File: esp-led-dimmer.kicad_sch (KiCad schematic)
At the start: 7 parts, among them J1 Barrel_Jack, J2 ESP-01, U1 LM2594M-3.3

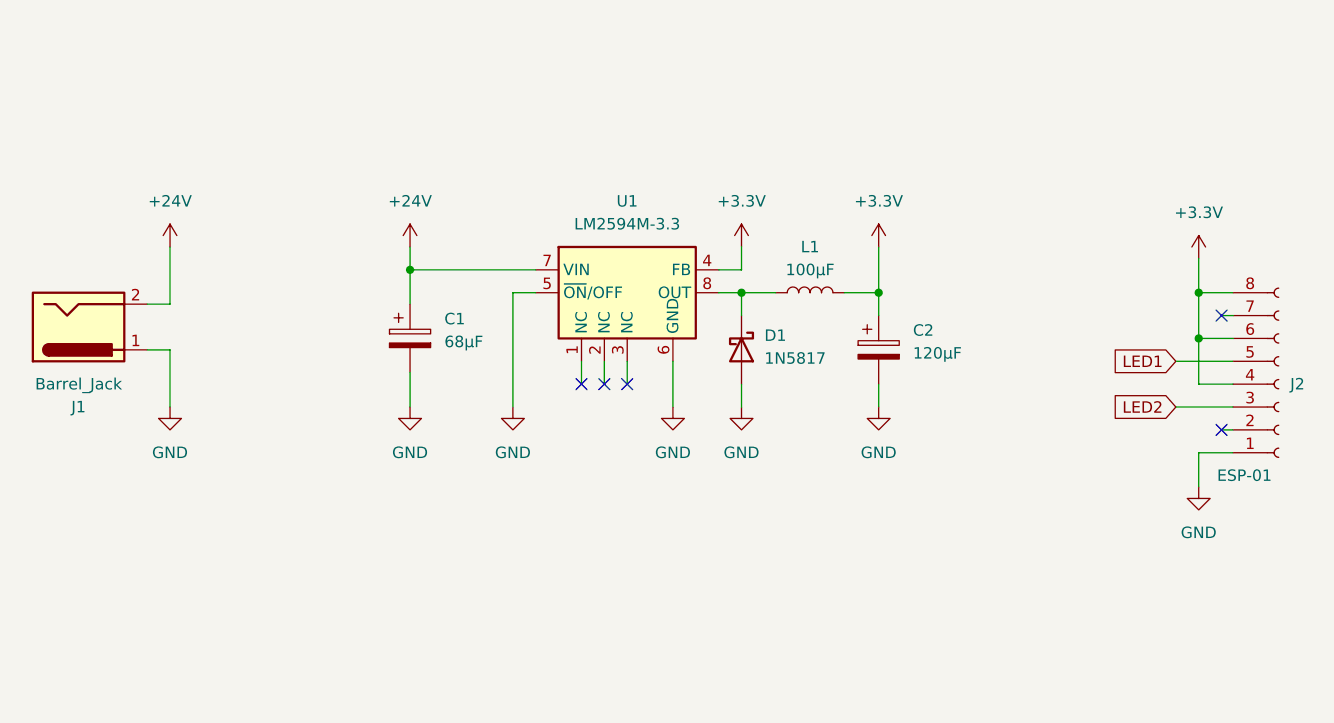
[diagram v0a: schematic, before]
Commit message: Add LED dimming circuit
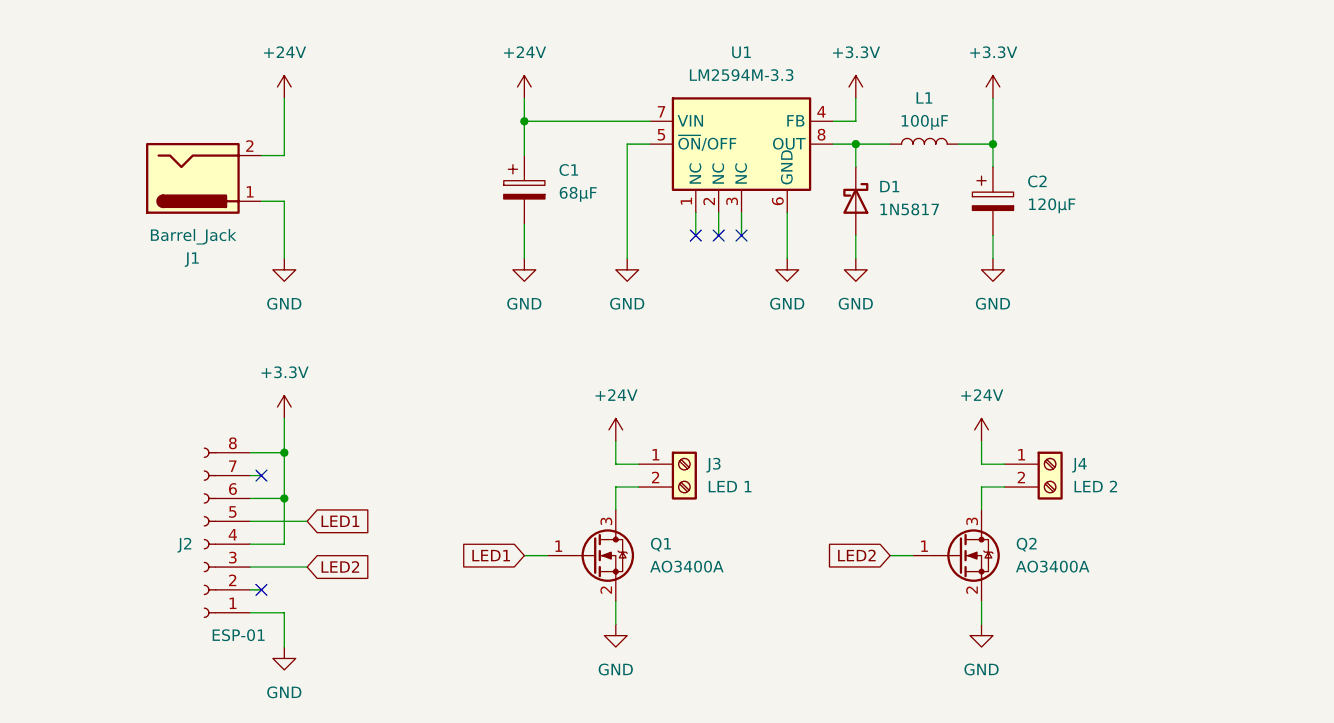
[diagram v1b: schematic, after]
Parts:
- added J3: LED 1, symbol Connector:Screw_Terminal_01x02
- added J4: LED 2, symbol Connector:Screw_Terminal_01x02
- added Q1, Q2: AO3400A, Package_TO_SOT_SMD:SOT-23, symbol Transistor_FET:AO3400A
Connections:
- net +24V: now also J3.1 (Pin_1), J4.1 (Pin_1)
- net GND: now also Q1.2 (S), Q2.2 (S)
- net LED1: now also Q1.1 (G)
- net LED2: now also Q2.1 (G)
- new net: J4.2 (Pin_2), Q2.3 (D)
- new net: J3.2 (Pin_2), Q1.3 (D)
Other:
- moved on the sheet: C1, C2, D1, J1, J2, L1, U1

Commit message: Replace LM2564 with TPS5430 for 3.3V power supply
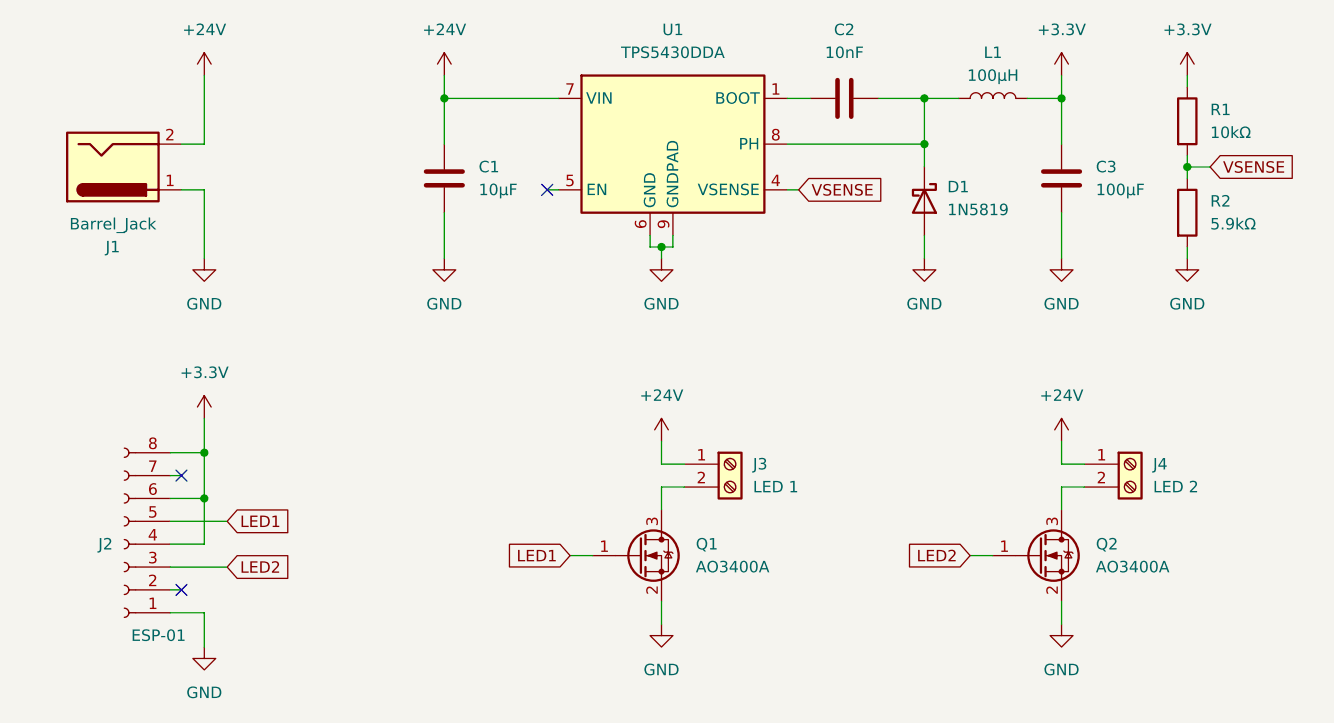
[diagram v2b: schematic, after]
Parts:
- removed C1: 68µF, symbol Device:C_Polarized
- removed C2: 120µF, symbol Device:C_Polarized
- removed D1: 1N5817, Diode_THT:D_DO-41_SOD81_P10.16mm_Horizontal, symbol Diode:1N5817
- removed U1: LM2594M-3.3, Package_SO:SOIC-8_3.9x4.9mm_P1.27mm, symbol Regulator_Switching:LM2594M-3.3
- added C1: 10µF, symbol Device:C
- added C2: 10nF, symbol Device:C
- added C3: 100µF, symbol Device:C
- added D1: 1N5819, Diode_THT:D_DO-41_SOD81_P10.16mm_Horizontal, symbol Diode:1N5819
- added R1: 10kΩ, symbol Device:R
- added R2: 5.9kΩ, symbol Device:R
- added U1: TPS5430DDA, Package_SO:TI_SO-PowerPAD-8_ThermalVias, symbol Regulator_Switching:TPS5430DDA
- L1: value 100µF -> 100µH
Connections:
- net +24V: now also C1.2, U1.7 (VIN)
- net +3.3V: now also C3.2, R1.1
- net GND: now also C1.1, C3.1, D1.2 (A), R2.2, U1.6 (GND), U1.9 (GNDPAD)
- net at L1.2: now also C2.2, D1.1 (K), U1.8 (PH)
- new net: C2.1, U1.1 (BOOT)
- new net VSENSE: R1.2, R2.1, U1.4 (VSENSE)
- no-connect marks 5 -> 3
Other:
- moved on the sheet: J1, J2, J3, J4, L1, Q1, Q2

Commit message: Assign footprints to schematic symbols
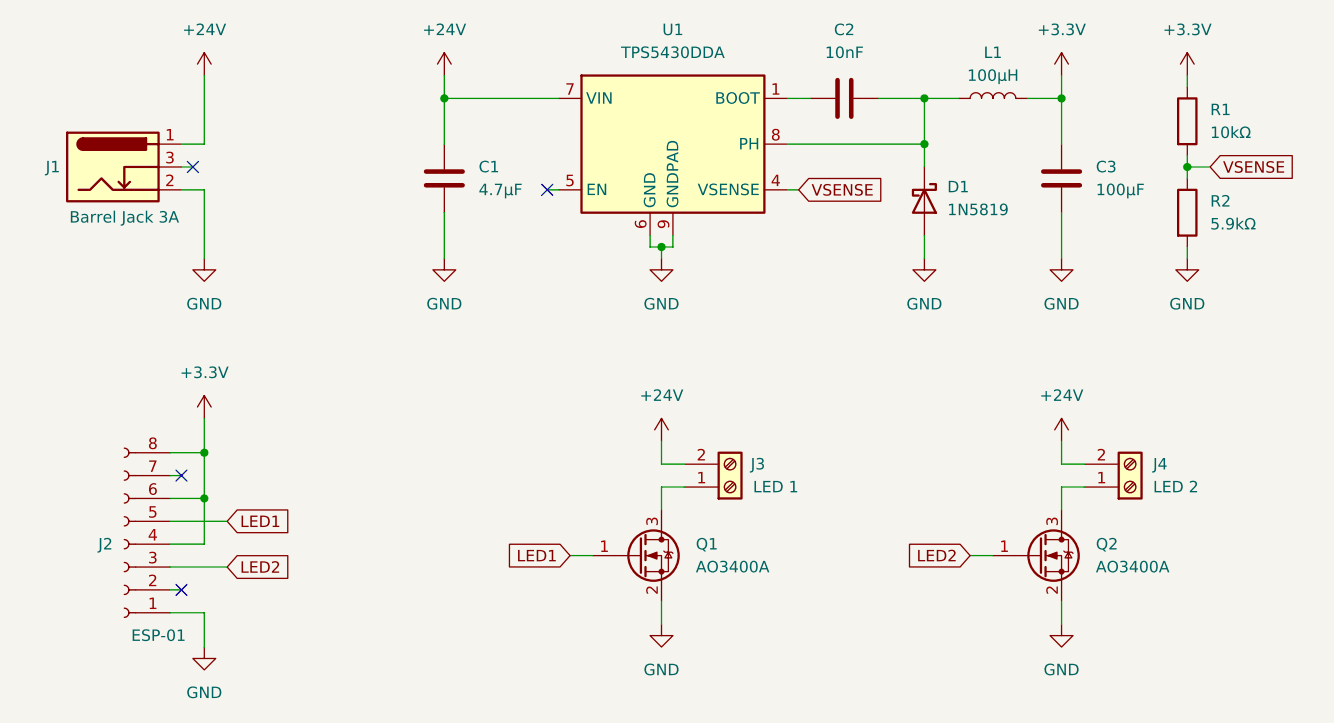
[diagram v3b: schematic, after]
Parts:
- removed J1: Barrel_Jack, symbol Connector:Barrel_Jack
- added J1: Barrel Jack 3A, Connector_BarrelJack:BarrelJack_Horizontal, symbol Connector:Barrel_Jack_Switch
- C1: value 10µF -> 4.7µF; footprint (none) -> Capacitor_SMD:C_0805_2012Metric
- C2: footprint (none) -> Capacitor_SMD:C_0402_1005Metric
- C3: footprint (none) -> Capacitor_SMD:C_1206_3216Metric
- D1: footprint Diode_THT:D_DO-41_SOD81_P10.16mm_Horizontal -> Diode_SMD:D_SOD-323
- J3, J4: footprint (none) -> TerminalBlock_Phoenix:TerminalBlock_Phoenix_MKDS-1,5-2_1x02_P5.00mm_Horizontal
- L1: footprint (none) -> Inductor_SMD:L_Bourns_SRN6045TA
- R1, R2: footprint (none) -> Resistor_SMD:R_0402_1005Metric
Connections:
- net +24V: now also J3.2 (Pin_2), J4.2 (Pin_2), J1.1; no longer J3.1 (Pin_1), J4.1 (Pin_1)
- net GND: now also J1.2
- net at Q2.3 (D): now also J4.1 (Pin_1); no longer J4.2 (Pin_2)
- net at Q1.3 (D): now also J3.1 (Pin_1); no longer J3.2 (Pin_2)
- no-connect marks 3 -> 4
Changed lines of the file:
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@@
+	)
+	(no_connect
+		(at 95.25 74.93)
 	)
 	(no_connect
@@
 		(pts
 			(xy 93.98 72.39) (xy 96.52 72.39)
+		)
+		(stroke
+			(width 0)
+			(type default)
+		)
+	)
+	(wire
+		(pts
+			(xy 95.25 74.93) (xy 93.98 74.93)
 		)
 		(stroke
@@
 			)
 		)
-		(property "Footprint" ""
+		(property "Footprint" "Capacitor_SMD:C_0402_1005Metric"
 			(at 171.45 66.3448 0)
 			(effects
@@
 				(path "/14bfeb0d-3bb3-4185-ac78-bdfa858bfae3"
 					(reference "C2")
+					(unit 1)
+				)
+			)
+		)
+	)
+	(symbol
+		(lib_id "Connector:Barrel_Jack_Switch")
+		(at 86.36 74.93 0)
+		(unit 1)
+		(exclude_from_sim no)
+		(in_bom yes)
+		(on_board yes)
+		(dnp no)
+		(property "Reference" "J1"
+			(at 80.518 74.93 0)
+			(effects
+				(font
+					(size 1.27 1.27)
+				)
+				(justify right)
+			)
+		)
+		(property "Value" "Barrel Jack 3A"
+			(at 93.726 80.518 0)
+			(effects
+				(font
+					(size 1.27 1.27)
+				)
+				(justify right)
+			)
+		)
+		(property "Footprint" "Connector_BarrelJack:BarrelJack_Horizontal"
+			(at 87.63 75.946 0)
+			(effects
+				(font
+					(size 1.27 1.27)
+				)
+				(hide yes)
+			)
+		)
+		(property "Datasheet" "~"
+			(at 87.63 75.946 0)
+			(effects
+				(font
+					(size 1.27 1.27)
+				)
+				(hide yes)
+			)
+		)
+		(property "Description" "DC Barrel Jack with an internal switch"
+			(at 86.36 74.93 0)
+			(effects
+				(font
+					(size 1.27 1.27)
+				)
+				(hide yes)
+			)
+		)
+		(pin "3"
+		)
+		(pin "2"
+		)
+		(pin "1"
+		)
+		(instances
+			(project ""
+				(path "/14bfeb0d-3bb3-4185-ac78-bdfa858bfae3"
+					(reference "J1")
 					(unit 1)
 				)
@@
 	(symbol
 		(lib_id "Connector:Screw_Terminal_01x02")
-		(at 199.39 107.95 0)
-		(unit 1)
-		(exclude_from_sim no)
-		(in_bom yes)
-		(on_board yes)
-		(dnp no)
-		(fields_autoplaced yes)
+		(at 199.39 110.49 0)
+		(mirror x)
+		(unit 1)
+		(exclude_from_sim no)
+		(in_bom yes)
+		(on_board yes)
+		(dnp no)
 		(property "Reference" "J4"
-			(at 201.93 107.9499 0)
+			(at 201.93 107.95 0)
 			(effects
 				(font
@@
 		)
 		(property "Value" "LED 2"
-			(at 201.93 110.4899 0)
+			(at 201.93 110.49 0)
 			(effects
 				(font
@@
 			)
 		)
-		(property "Footprint" ""
-			(at 199.39 107.95 0)
+		(property "Footprint" "TerminalBlock_Phoenix:TerminalBlock_Phoenix_MKDS-1,5-2_1x02_P5.00mm_Horizontal"
+			(at 199.39 110.49 0)
 			(effects
 				(font
@@
 		)
 		(property "Datasheet" "~"
-			(at 199.39 107.95 0)
+			(at 199.39 110.49 0)
 			(effects
 				(font
@@
 		)
 		(property "Description" "Generic screw terminal, single row, 01x02, script generated (kicad-library-utils/schlib/autogen/connector/)"
-			(at 199.39 107.95 0)
+			(at 199.39 110.49 0)
 			(effects
 				(font
@@
 			)
 		)
-		(property "Footprint" "Diode_THT:D_DO-41_SOD81_P10.16mm_Horizontal"
+		(property "Footprint" "Diode_SMD:D_SOD-323"
 			(at 172.085 78.74 0)
 			(effects
@@
 			)
 		)
-		(property "Footprint" ""
+		(property "Footprint" "Resistor_SMD:R_0402_1005Metric"
 			(at 203.962 69.85 90)
 			(effects
@@
 			)
 		)
-		(property "Footprint" ""
+		(property "Footprint" "Inductor_SMD:L_Bourns_SRN6045TA"
 			(at 184.15 67.31 0)
 			(effects
@@
 	(symbol
 		(lib_id "Connector:Screw_Terminal_01x02")
-		(at 154.94 107.95 0)
-		(unit 1)
-		(exclude_from_sim no)
-		(in_bom yes)
-		(on_board yes)
-		(dnp no)
-		(fields_autoplaced yes)
+		(at 154.94 110.49 0)
+		(mirror x)
+		(unit 1)
+		(exclude_from_sim no)
+		(in_bom yes)
+		(on_board yes)
+		(dnp no)
 		(property "Reference" "J3"
-			(at 157.48 107.9499 0)
+			(at 157.226 107.95 0)
 			(effects
 				(font
@@
 		)
 		(property "Value" "LED 1"
-			(at 157.48 110.4899 0)
+			(at 157.48 110.49 0)
 			(effects
 				(font
@@
 			)
 		)
-		(property "Footprint" ""
-			(at 154.94 107.95 0)
+		(property "Footprint" "TerminalBlock_Phoenix:TerminalBlock_Phoenix_MKDS-1,5-2_1x02_P5.00mm_Horizontal"
+			(at 154.94 110.49 0)
 			(effects
 				(font
@@
 		)
 		(property "Datasheet" "~"
-			(at 154.94 107.95 0)
+			(at 154.94 110.49 0)
 			(effects
 				(font
@@
 		)
 		(property "Description" "Generic screw terminal, single row, 01x02, script generated (kicad-library-utils/schlib/autogen/connector/)"
-			(at 154.94 107.95 0)
+			(at 154.94 110.49 0)
 			(effects
 				(font
@@
 			)
 		)
-		(property "Value" "10µF"
+		(property "Value" "4.7µF"
 			(at 127 77.4699 0)
 			(effects
@@
 			)
 		)
-		(property "Footprint" ""
+		(property "Footprint" "Capacitor_SMD:C_0805_2012Metric"
 			(at 122.2248 72.39 0)
 			(effects
@@
 			)
 		)
-		(property "Footprint" ""
+		(property "Footprint" "Capacitor_SMD:C_1206_3216Metric"
 			(at 190.8048 72.39 0)
 			(effects
@@
 	)
 	(symbol
-		(lib_id "Connector:Barrel_Jack")
-		(at 86.36 74.93 0)
-		(mirror x)
-		(unit 1)
-		(exclude_from_sim no)
-		(in_bom yes)
-		(on_board yes)
-		(dnp no)
-		(fields_autoplaced yes)
-		(property "Reference" "J1"
-			(at 86.36 83.82 0)
-			(effects
-				(font
-					(size 1.27 1.27)
-				)
-			)
-		)
-		(property "Value" "Barrel_Jack"
-			(at 86.36 81.28 0)
-			(effects
-				(font
-					(size 1.27 1.27)
-				)
-			)
-		)
-		(property "Footprint" ""
-			(at 87.63 73.914 0)
-			(effects
-				(font
-					(size 1.27 1.27)
-				)
-				(hide yes)
-			)
-		)
-		(property "Datasheet" "~"
-			(at 87.63 73.914 0)
-			(effects
-				(font
-					(size 1.27 1.27)
-				)
-				(hide yes)
-			)
-		)
-		(property "Description" "DC Barrel Jack"
-			(at 86.36 74.93 0)
-			(effects
-				(font
-					(size 1.27 1.27)
-				)
-				(hide yes)
-			)
-		)
-		(pin "1"
-		)
-		(pin "2"
-		)
-		(instances
-			(project ""
-				(path "/14bfeb0d-3bb3-4185-ac78-bdfa858bfae3"
-					(reference "J1")
-					(unit 1)
-				)
-			)
-		)
-	)
-	(symbol
 		(lib_id "Device:R")
 		(at 205.74 80.01 0)
@@
 			)
 		)
-		(property "Footprint" ""
+		(property "Footprint" "Resistor_SMD:R_0402_1005Metric"
 			(at 203.962 80.01 90)
 			(effects
